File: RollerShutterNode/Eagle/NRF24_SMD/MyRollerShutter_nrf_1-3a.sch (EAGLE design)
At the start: 61 parts, among them IC1 ATMega-328, IC2 AT25DF512C-SSHN-B, IC3 MCP1703CB, IC4 ACS712_5A, IC5 ATSHA204A, IC6 LM321, IC7 MDC3105DMT1, IC8 DS1820, J1 SCREW-TERMINAL-2P-3470110P1, J2 SCREW-TERMINAL-2P-3470110P1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

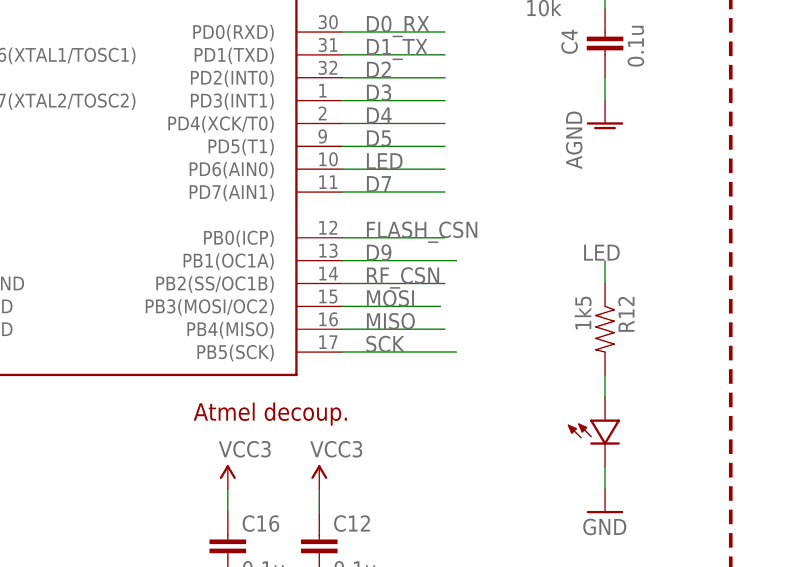
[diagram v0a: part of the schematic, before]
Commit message: nrf24 minor fix
CSN was not connected in pcb! whereas it was in schematics..
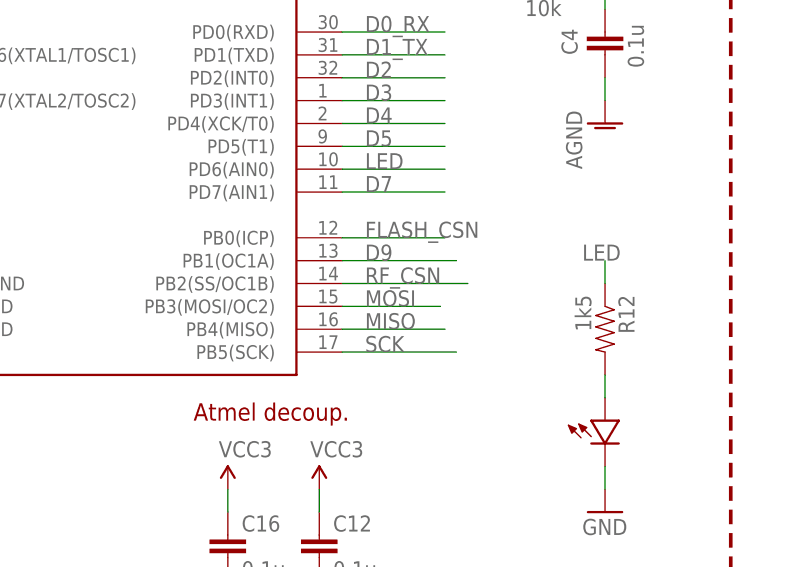
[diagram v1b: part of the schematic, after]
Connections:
- removed net N$8: NRF_SMD.CSN
- net RF_CSN: now also NRF_SMD.CSN
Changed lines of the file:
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@@
 <grid distance="0.1" unitdist="inch" unit="inch" style="lines" multiple="1" display="no" altdistance="0.01" altunitdist="inch" altunit="inch"/>
 <layers>
-<layer number="1" name="Top" color="4" fill="1" visible="no" active="no"/>
-<layer number="2" name="Route2" color="1" fill="3" visible="no" active="no"/>
-<layer number="3" name="Route3" color="4" fill="3" visible="no" active="no"/>
-<layer number="4" name="Route4" color="1" fill="4" visible="no" active="no"/>
-<layer number="5" name="Route5" color="4" fill="4" visible="no" active="no"/>
-<layer number="6" name="Route6" color="1" fill="8" visible="no" active="no"/>
-<layer number="7" name="Route7" color="4" fill="8" visible="no" active="no"/>
-<layer number="8" name="Route8" color="1" fill="2" visible="no" active="no"/>
-<layer number="9" name="Route9" color="4" fill="2" visible="no" active="no"/>
-<layer number="10" name="Route10" color="1" fill="7" visible="no" active="no"/>
-<layer number="11" name="Route11" color="4" fill="7" visible="no" active="no"/>
-<layer number="12" name="Route12" color="1" fill="5" visible="no" active="no"/>
-<layer number="13" name="Route13" color="4" fill="5" visible="no" active="no"/>
-<layer number="14" name="Route14" color="1" fill="6" visible="no" active="no"/>
-<layer number="15" name="Route15" color="4" fill="6" visible="no" active="no"/>
-<layer number="16" name="Bottom" color="1" fill="1" visible="no" active="no"/>
-<layer number="17" name="Pads" color="2" fill="1" visible="no" active="no"/>
-<layer number="18" name="Vias" color="2" fill="1" visible="no" active="no"/>
-<layer number="19" name="Unrouted" color="6" fill="1" visible="no" active="no"/>
-<layer number="20" name="Dimension" color="15" fill="1" visible="no" active="no"/>
-<layer number="21" name="tPlace" color="7" fill="1" visible="no" active="no"/>
-<layer number="22" name="bPlace" color="7" fill="1" visible="no" active="no"/>
-<layer number="23" name="tOrigins" color="15" fill="1" visible="no" active="no"/>
-<layer number="24" name="bOrigins" color="15" fill="1" visible="no" active="no"/>
-<layer number="25" name="tNames" color="7" fill="1" visible="no" active="no"/>
-<layer number="26" name="bNames" color="7" fill="1" visible="no" active="no"/>
-<layer number="27" name="tValues" color="7" fill="1" visible="no" active="no"/>
-<layer number="28" name="bValues" color="7" fill="1" visible="no" active="no"/>
+<layer number="1" name="Top" color="4" fill="1" visible="yes" active="no"/>
+<layer number="2" name="Route2" color="1" fill="3" visible="yes" active="no"/>
+<layer number="3" name="Route3" color="4" fill="3" visible="yes" active="no"/>
+<layer number="4" name="Route4" color="1" fill="4" visible="yes" active="no"/>
+<layer number="5" name="Route5" color="4" fill="4" visible="yes" active="no"/>
+<layer number="6" name="Route6" color="1" fill="8" visible="yes" active="no"/>
+<layer number="7" name="Route7" color="4" fill="8" visible="yes" active="no"/>
+<layer number="8" name="Route8" color="1" fill="2" visible="yes" active="no"/>
+<layer number="9" name="Route9" color="4" fill="2" visible="yes" active="no"/>
+<layer number="10" name="Route10" color="1" fill="7" visible="yes" active="no"/>
+<layer number="11" name="Route11" color="4" fill="7" visible="yes" active="no"/>
+<layer number="12" name="Route12" color="1" fill="5" visible="yes" active="no"/>
+<layer number="13" name="Route13" color="4" fill="5" visible="yes" active="no"/>
+<layer number="14" name="Route14" color="1" fill="6" visible="yes" active="no"/>
+<layer number="15" name="Route15" color="4" fill="6" visible="yes" active="no"/>
+<layer number="16" name="Bottom" color="1" fill="1" visible="yes" active="no"/>
+<layer number="17" name="Pads" color="2" fill="1" visible="yes" active="no"/>
+<layer number="18" name="Vias" color="2" fill="1" visible="yes" active="no"/>
+<layer number="19" name="Unrouted" color="6" fill="1" visible="yes" active="no"/>
+<layer number="20" name="Dimension" color="15" fill="1" visible="yes" active="no"/>
+<layer number="21" name="tPlace" color="7" fill="1" visible="yes" active="no"/>
+<layer number="22" name="bPlace" color="7" fill="1" visible="yes" active="no"/>
+<layer number="23" name="tOrigins" color="15" fill="1" visible="yes" active="no"/>
+<layer number="24" name="bOrigins" color="15" fill="1" visible="yes" active="no"/>
+<layer number="25" name="tNames" color="7" fill="1" visible="yes" active="no"/>
+<layer number="26" name="bNames" color="7" fill="1" visible="yes" active="no"/>
+<layer number="27" name="tValues" color="7" fill="1" visible="yes" active="no"/>
+<layer number="28" name="bValues" color="7" fill="1" visible="yes" active="no"/>
 <layer number="29" name="tStop" color="7" fill="3" visible="no" active="no"/>
 <layer number="30" name="bStop" color="7" fill="6" visible="no" active="no"/>
@@
 <layer number="35" name="tGlue" color="7" fill="4" visible="no" active="no"/>
 <layer number="36" name="bGlue" color="7" fill="5" visible="no" active="no"/>
-<layer number="37" name="tTest" color="7" fill="1" visible="no" active="no"/>
-<layer number="38" name="bTest" color="7" fill="1" visible="no" active="no"/>
+<layer number="37" name="tTest" color="7" fill="1" visible="yes" active="no"/>
+<layer number="38" name="bTest" color="7" fill="1" visible="yes" active="no"/>
 <layer number="39" name="tKeepout" color="4" fill="11" visible="no" active="no"/>
 <layer number="40" name="bKeepout" color="1" fill="11" visible="no" active="no"/>
@@
 <layer number="44" name="Drills" color="7" fill="1" visible="no" active="no"/>
 <layer number="45" name="Holes" color="7" fill="1" visible="no" active="no"/>
-<layer number="46" name="Milling" color="3" fill="1" visible="no" active="no"/>
-<layer number="47" name="Measures" color="7" fill="1" visible="no" active="no"/>
-<layer number="48" name="Document" color="7" fill="1" visible="no" active="no"/>
-<layer number="49" name="Reference" color="7" fill="1" visible="no" active="no"/>
-<layer number="50" name="dxf" color="7" fill="1" visible="no" active="no"/>
-<layer number="51" name="tDocu" color="7" fill="1" visible="no" active="no"/>
-<layer number="52" name="bDocu" color="7" fill="1" visible="no" active="no"/>
-<layer number="53" name="tGND_GNDA" color="7" fill="9" visible="no" active="no"/>
-<layer number="54" name="bGND_GNDA" color="1" fill="9" visible="no" active="no"/>
-<layer number="56" name="wert" color="7" fill="1" visible="no" active="no"/>
-<layer number="57" name="tCAD" color="7" fill="1" visible="no" active="no"/>
-<layer number="58" name="b3D" color="7" fill="1" visible="no" active="no"/>
-<layer number="59" name="tCarbon" color="7" fill="1" visible="no" active="no"/>
-<layer number="60" name="bCarbon" color="7" fill="1" visible="no" active="no"/>
+<layer number="46" name="Milling" color="3" fill="1" visible="yes" active="no"/>
+<layer number="47" name="Measures" color="7" fill="1" visible="yes" active="no"/>
+<layer number="48" name="Document" color="7" fill="1" visible="yes" active="no"/>
+<layer number="49" name="Reference" color="7" fill="1" visible="yes" active="no"/>
+<layer number="50" name="dxf" color="7" fill="1" visible="yes" active="no"/>
+<layer number="51" name="tDocu" color="7" fill="1" visible="yes" active="no"/>
+<layer number="52" name="bDocu" color="7" fill="1" visible="yes" active="no"/>
+<layer number="53" name="tGND_GNDA" color="7" fill="9" visible="yes" active="no"/>
+<layer number="54" name="bGND_GNDA" color="1" fill="9" visible="yes" active="no"/>
+<layer number="56" name="wert" color="7" fill="1" visible="yes" active="no"/>
+<layer number="57" name="tCAD" color="7" fill="1" visible="yes" active="no"/>
+<layer number="58" name="b3D" color="7" fill="1" visible="yes" active="no"/>
+<layer number="59" name="tCarbon" color="7" fill="1" visible="yes" active="no"/>
+<layer number="60" name="bCarbon" color="7" fill="1" visible="yes" active="no"/>
 <layer number="90" name="Modules" color="5" fill="1" visible="yes" active="yes"/>
 <layer number="91" name="Nets" color="2" fill="1" visible="yes" active="yes"/>
@@
 <net name="RF_CSN" class="0">
 <segment>
-<wire x1="16.51" y1="-68.58" x2="27.94" y2="-68.58" width="0.1524" layer="91"/>
+<wire x1="16.51" y1="-68.58" x2="30.48" y2="-68.58" width="0.1524" layer="91"/>
 <label x="19.05" y="-68.58" size="1.778" layer="95"/>
 <pinref part="IC1" gate="G$1" pin="PB2(SS/OC1B)"/>
@@
 <pinref part="R14" gate="G$1" pin="1"/>
 <wire x1="266.7" y1="-27.94" x2="266.7" y2="-30.48" width="0.1524" layer="91"/>
+</segment>
+<segment>
+<pinref part="NRF_SMD" gate="G$1" pin="CSN"/>
+<wire x1="297.18" y1="-38.1" x2="284.48" y2="-38.1" width="0.1524" layer="91"/>
 <label x="284.48" y="-38.1" size="1.778" layer="95"/>
 </segment>
@@
 </segment>
 </net>
-<net name="N$8" class="0">
-<segment>
-<pinref part="NRF_SMD" gate="G$1" pin="CSN"/>
-<wire x1="297.18" y1="-38.1" x2="284.48" y2="-38.1" width="0.1524" layer="91"/>
-</segment>
-</net>
